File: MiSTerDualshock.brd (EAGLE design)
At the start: 99.8 x 49.8 mm, 21 parts, among them K1 692121030100

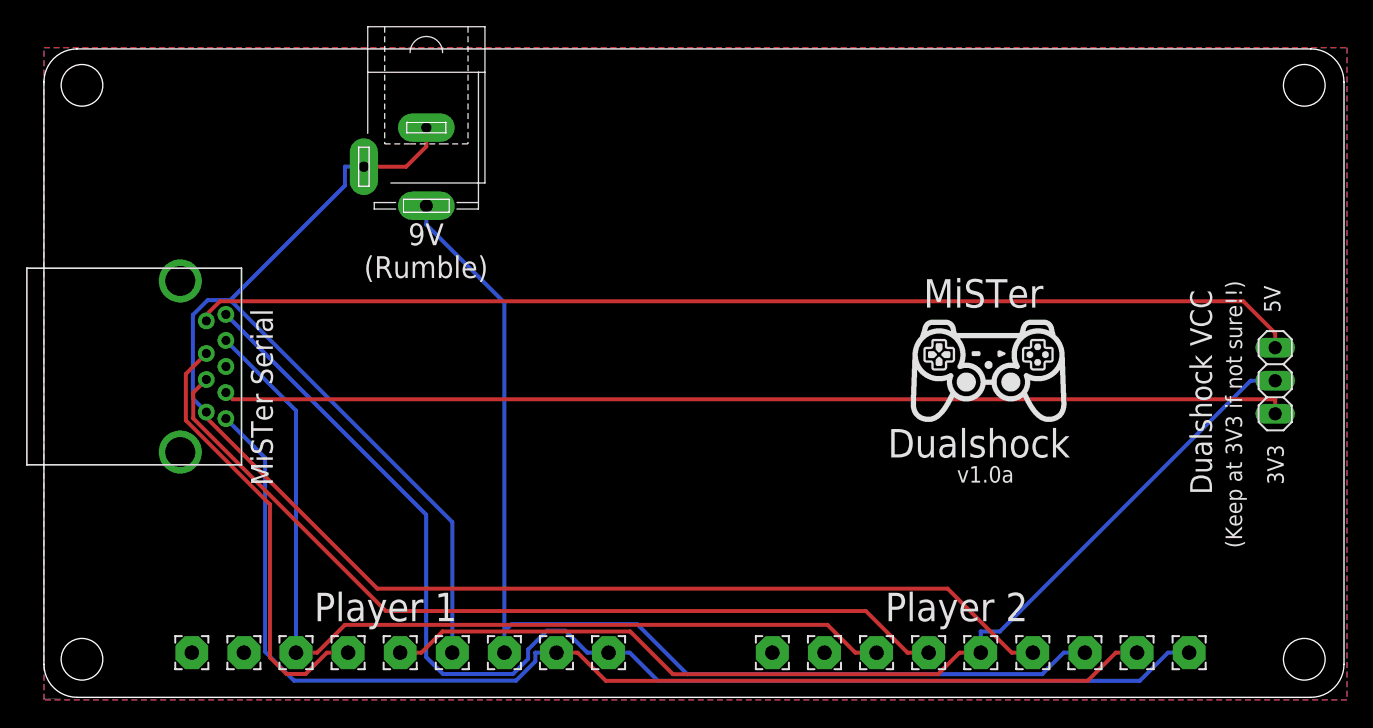
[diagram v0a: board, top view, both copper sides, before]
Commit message: Added pull-up resistor to DAT line
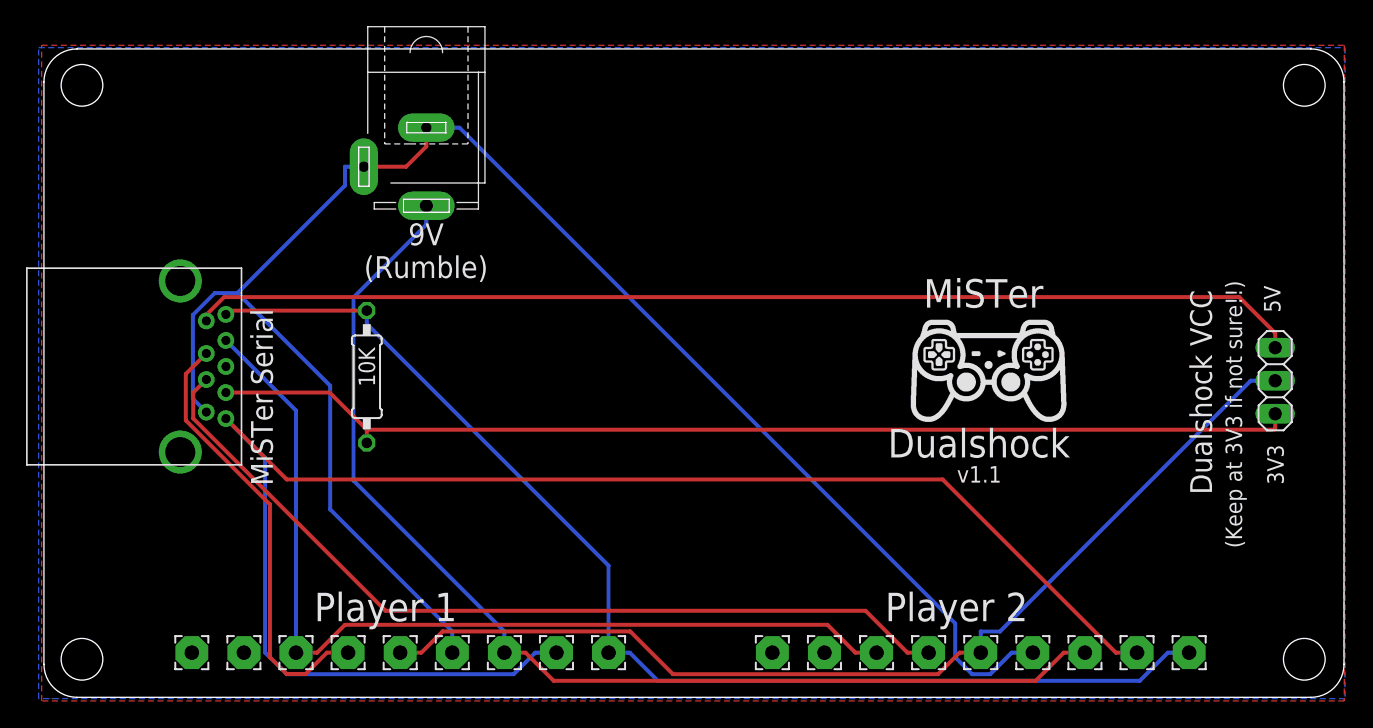
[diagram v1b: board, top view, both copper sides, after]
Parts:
- added R1: 10K, resistor:0207/10
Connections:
- net 3V3: now also R1.2
- net DAT: now also R1.1
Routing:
- net CMD: track 90.1 -> 120.4 mm
- net GND: track 138.9 -> 134.1 mm
- net DAT: track 96.1 -> 91.3 mm
- net 9V: track 83.9 -> 87.8 mm
- net 3V3: track 81.9 -> 83.9 mm
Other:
- board text added: "v1.1"
- board text removed: "v1.0a"

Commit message: Version 1.2
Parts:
- added R2, R3, R4, R5: 10K, resistor:0207/10
- moved R1 1.49 mm to (23.5, 25.3)
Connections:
- net 3V3: now also R2.2, R3.2, R4.2, R5.2
- net ATT1: now also R2.1
- net ATT2: now also R5.1
- net CLK: now also R1.1
- net CMD: now also R4.1
- net DAT: now also R3.1; no longer R1.1
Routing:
- net CLK: track 72.5 -> 121.9 mm
- net CMD: track 120.4 -> 99.1 mm
- net ATT1: track 33.9 -> 47.8 mm
- net ATT2: track 67.3 -> 77.7 mm
- net DAT: track 91.3 -> 98.9 mm
- net 9V: track 87.8 -> 84.2 mm
- net GND: track 134.1 -> 130.7 mm
- net 5V: track 85.4 -> 87.0 mm
- net VCC: track 79.5 -> 78.6 mm
- net 3V3: track 83.9 -> 83.2 mm
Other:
- board text added: "v1.2"
- board text removed: "v1.1"
